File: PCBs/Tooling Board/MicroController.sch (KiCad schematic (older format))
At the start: 20 parts, among them J201 Conn_02x05_Odd_Even, SW201 SW_Push, U201 ATSAMD21E18A-MFTCT-ND, Y201 32.7680kHz

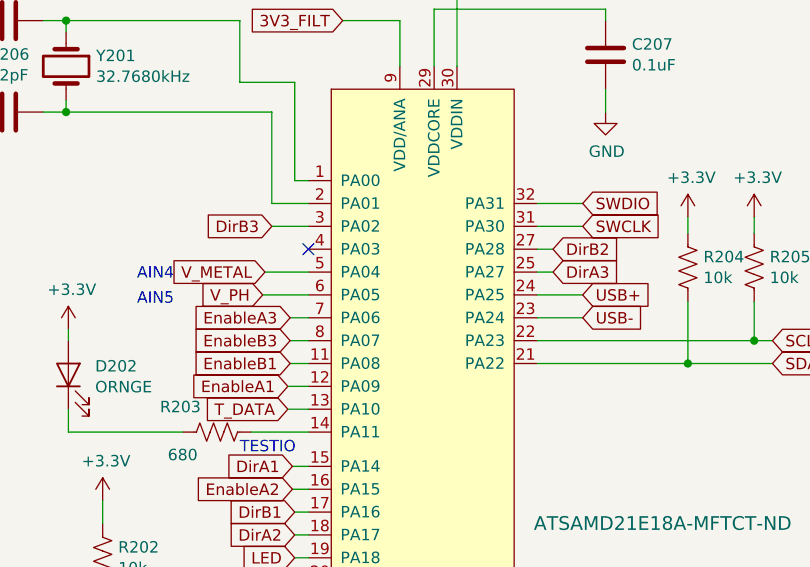
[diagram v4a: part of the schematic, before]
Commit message: Removed 3rd DC Motor Driver
-Can only do 4 DC motors now, not enough board space
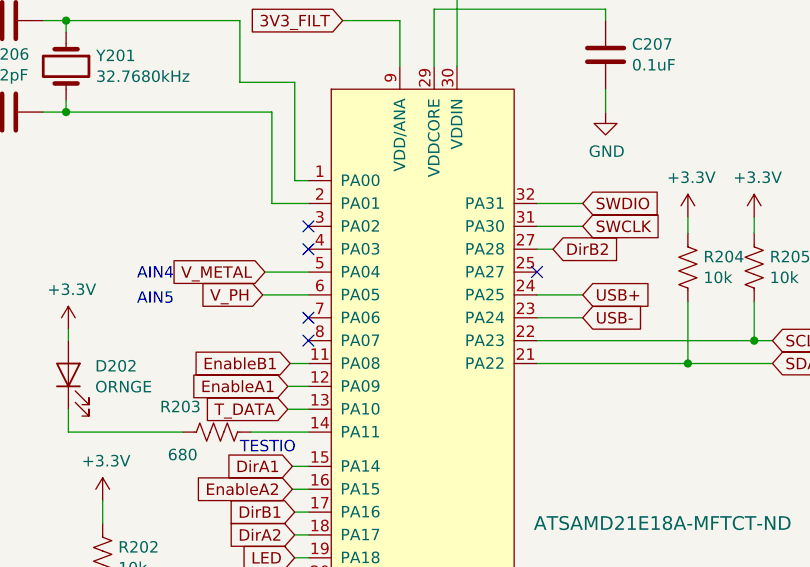
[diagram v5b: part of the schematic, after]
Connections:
- net DirA3: no longer names the net of U201.25 (PA27)
- net DirB3: no longer names the net of U201.3 (PA02)
- net EnableA3: no longer names the net of U201.7 (PA06)
- net EnableB3: no longer names the net of U201.8 (PA07)
- no-connect marks 5 -> 9
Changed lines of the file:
@@
 $Descr A4 11693 8268
 encoding utf-8
-Sheet 2 8
+Sheet 2 7
 Title ""
 Date ""
@@
 	5940 4100 6000 4100
 Wire Wire Line
-	7000 2750 7070 2750
-Wire Wire Line
 	7000 2650 7070 2650
 Text GLabel 7070 2650 2    50   Input ~ 0
 DirB2
-Text GLabel 7070 2750 2    50   Input ~ 0
-DirA3
-Text GLabel 5920 2950 0    50   Input ~ 0
-EnableA3
-Text GLabel 5920 3050 0    50   Input ~ 0
-EnableB3
-Wire Wire Line
-	5920 3050 6000 3050
-Wire Wire Line
-	6000 2950 5920 2950
 Text GLabel 5940 3900 0    50   Input ~ 0
 DirA2
 Wire Wire Line
 	5810 2750 6000 2750
-Text GLabel 5840 2550 0    50   Input ~ 0
-DirB3
-Wire Wire Line
-	5840 2550 6000 2550
 NoConn ~ 6000 2650
 Wire Wire Line
@@
 Text Notes 5250 2790 0    50   ~ 0
 AIN4
+NoConn ~ 6000 2950
+NoConn ~ 6000 3050
+NoConn ~ 7000 2750
+NoConn ~ 6000 2550
 $EndSCHEMATC

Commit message: Almost Finished
-Still going, help
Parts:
- C201, C202, C203, C204, C207: footprint Capacitors_SMD:C_0805_HandSoldering -> Capacitors_SMD:C_0805
- C205, C206: footprint Capacitors_SMD:C_0603_HandSoldering -> Capacitors_SMD:C_0603
- D201, D202: footprint LEDs:LED_0805_HandSoldering -> LEDs:LED_0805
- R201, R202, R203, R204, R205: footprint Resistors_SMD:R_0805_HandSoldering -> Resistors_SMD:R_0805
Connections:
- net +5V: no longer L202.2
- new net +5V_IN: L202.2
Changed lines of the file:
@@
 F 0 "R202" H 5168 4046 50  0000 L CNN
 F 1 "10k" H 5168 3955 50  0000 L CNN
-F 2 "Resistors_SMD:R_0805_HandSoldering" V 5140 3990 50  0001 C CNN
+F 2 "Resistors_SMD:R_0805" V 5140 3990 50  0001 C CNN
 F 3 "RNCP0805FTD10K0CT-ND" H 5100 4000 50  0001 C CNN
 	1    5100 4000
@@
 F 0 "C201" H 2365 1496 50  0000 L CNN
 F 1 "10uF" H 2365 1405 50  0000 L CNN
-F 2 "Capacitors_SMD:C_0805_HandSoldering" H 2288 1300 50  0001 C CNN
+F 2 "Capacitors_SMD:C_0805" H 2288 1300 50  0001 C CNN
 F 3 "490-7201-1-ND" H 2250 1450 50  0001 C CNN
 	1    2250 1450
@@
 F 0 "C202" H 2815 1496 50  0000 L CNN
 F 1 "0.1uF" H 2815 1405 50  0000 L CNN
-F 2 "Capacitors_SMD:C_0805_HandSoldering" H 2738 1300 50  0001 C CNN
+F 2 "Capacitors_SMD:C_0805" H 2738 1300 50  0001 C CNN
 F 3 "1276-1258-1-ND" H 2700 1450 50  0001 C CNN
 	1    2700 1450
@@
 F 0 "C203" H 2915 2896 50  0000 L CNN
 F 1 "10uF" H 2915 2805 50  0000 L CNN
-F 2 "Capacitors_SMD:C_0805_HandSoldering" H 2838 2700 50  0001 C CNN
+F 2 "Capacitors_SMD:C_0805" H 2838 2700 50  0001 C CNN
 F 3 "490-7201-1-ND" H 2800 2850 50  0001 C CNN
 	1    2800 2850
@@
 F 0 "C204" H 3365 2896 50  0000 L CNN
 F 1 "1uF" H 3365 2805 50  0000 L CNN
-F 2 "Capacitors_SMD:C_0805_HandSoldering" H 3288 2700 50  0001 C CNN
+F 2 "Capacitors_SMD:C_0805" H 3288 2700 50  0001 C CNN
 F 3 "1276-6524-1-ND" H 3250 2850 50  0001 C CNN
 	1    3250 2850
@@
 F 0 "R201" H 3868 2896 50  0000 L CNN
 F 1 "330" H 3868 2805 50  0000 L CNN
-F 2 "Resistors_SMD:R_0805_HandSoldering" V 3840 2840 50  0001 C CNN
+F 2 "Resistors_SMD:R_0805" V 3840 2840 50  0001 C CNN
 F 3 "RHM330DCT-ND" H 3800 2850 50  0001 C CNN
 	1    3800 2850
@@
 F 0 "D201" V 3838 3182 50  0000 R CNN
 F 1 "RED" V 3747 3182 50  0000 R CNN
-F 2 "LEDs:LED_0805_HandSoldering" H 3800 3300 50  0001 C CNN
+F 2 "LEDs:LED_0805" H 3800 3300 50  0001 C CNN
 F 3 "732-4984-1-ND" H 3800 3300 50  0001 C CNN
 	1    3800 3300
@@
 F 0 "C205" V 4438 1650 50  0000 C CNN
 F 1 "22pF" V 4529 1650 50  0000 C CNN
-F 2 "Capacitors_SMD:C_0603_HandSoldering" H 4728 1500 50  0001 C CNN
+F 2 "Capacitors_SMD:C_0603" H 4728 1500 50  0001 C CNN
 F 3 "311-3925-1-ND" H 4690 1650 50  0001 C CNN
 	1    4690 1650
@@
 F 0 "C206" V 4438 2050 50  0000 C CNN
 F 1 "22pF" V 4529 2050 50  0000 C CNN
-F 2 "Capacitors_SMD:C_0603_HandSoldering" H 4728 1900 50  0001 C CNN
+F 2 "Capacitors_SMD:C_0603" H 4728 1900 50  0001 C CNN
 F 3 "311-3925-1-ND" H 4690 2050 50  0001 C CNN
 	1    4690 2050
@@
 F 0 "C207" H 7415 1846 50  0000 L CNN
 F 1 "0.1uF" H 7415 1755 50  0000 L CNN
-F 2 "Capacitors_SMD:C_0805_HandSoldering" H 7338 1650 50  0001 C CNN
+F 2 "Capacitors_SMD:C_0805" H 7338 1650 50  0001 C CNN
 F 3 "1276-1258-1-ND" H 7300 1800 50  0001 C CNN
 	1    7300 1800
@@
 F 0 "R203" V 5490 3290 50  0000 C CNN
 F 1 "680" V 5700 3300 50  0000 C CNN
-F 2 "Resistors_SMD:R_0805_HandSoldering" V 5640 3440 50  0001 C CNN
+F 2 "Resistors_SMD:R_0805" V 5640 3440 50  0001 C CNN
 F 3 "RHM680DCT-ND" H 5600 3450 50  0001 C CNN
 	1    5600 3450
@@
 F 0 "D202" V 4988 3083 50  0000 R CNN
 F 1 "ORNGE" V 4897 3083 50  0000 R CNN
-F 2 "LEDs:LED_0805_HandSoldering" H 4950 3200 50  0001 C CNN
+F 2 "LEDs:LED_0805" H 4950 3200 50  0001 C CNN
 F 3 "160-1413-1-ND" H 4950 3200 50  0001 C CNN
 	1    4950 3200
@@
 	1100 2800 1950 2800
 Text HLabel 1100 2500 0    50   Input ~ 0
-+5V
++5V_IN
 Text HLabel 1100 2700 0    50   BiDi ~ 0
 USB+
@@
 F 0 "R204" H 7728 2776 50  0000 L CNN
 F 1 "10k" H 7728 2685 50  0000 L CNN
-F 2 "Resistors_SMD:R_0805_HandSoldering" V 7700 2720 50  0001 C CNN
+F 2 "Resistors_SMD:R_0805" V 7700 2720 50  0001 C CNN
 F 3 "" H 7660 2730 50  0001 C CNN
 	1    7660 2730
@@
 F 0 "R205" H 8018 2776 50  0000 L CNN
 F 1 "10k" H 8018 2685 50  0000 L CNN
-F 2 "Resistors_SMD:R_0805_HandSoldering" V 7990 2720 50  0001 C CNN
+F 2 "Resistors_SMD:R_0805" V 7990 2720 50  0001 C CNN
 F 3 "" H 7950 2730 50  0001 C CNN
 	1    7950 2730
